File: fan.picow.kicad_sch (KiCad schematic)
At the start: 41 parts, among them U1 PicoW

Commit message: pop stashed changes
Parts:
- removed C2: 0.1uF, Capacitor_SMD:C_0603_1608Metric_Pad1.08x0.95mm_HandSolder, symbol Device:C
- removed D4: LED 12V, LED_SMD:LED_0805_2012Metric_Pad1.15x1.40mm_HandSolder, symbol Device:LED
- removed D8: LED 5V, LED_SMD:LED_0805_2012Metric_Pad1.15x1.40mm_HandSolder, symbol Device:LED
- removed D9: 1N5819, Diode_SMD:D_SMA_Handsoldering, symbol Diode:1N5819
- removed R16: 10K, Resistor_SMD:R_0603_1608Metric_Pad0.98x0.95mm_HandSolder, symbol Device:R
- removed R8: 49.9K, Resistor_SMD:R_0603_1608Metric_Pad0.98x0.95mm_HandSolder, symbol Device:R
- added C10: 0.1uF, Capacitor_SMD:C_0603_1608Metric_Pad1.08x0.95mm_HandSolder, symbol Device:C
- added D9: CDBW140-G, Diode_SMD:D_SOD-123F, symbol CDBW140-G:CDBW140-G
- added LS1: CMT-7525-80-SMT-TR, footprints descargados:XDCR_CMT-7525-80-SMT-TR, symbol CMT-7525-80-SMT-TR:CMT-7525-80-SMT-TR
- added Q1: AOD4184A, footprints descargados:DPAK228P994X240-4N, symbol AOD4184A:AOD4184A
- added Q2: BSS138, Package_TO_SOT_SMD:SOT-23, symbol Transistor_FET:BSS138
- added R23: 1k, Resistor_SMD:R_0603_1608Metric_Pad0.98x0.95mm_HandSolder, symbol Device:R
- added SW1: EG1257, footprints descargados:EG1257, symbol EG1257:EG1257
- D1, D7: footprint LED_SMD:LED_0805_2012Metric_Pad1.15x1.40mm_HandSolder -> digikey-footprints:0805; symbol Device:LED -> dk_LED-Indication-Discrete:LG_R971-KN-1; Category (none) -> Optoelectronics; DK_Datasheet_Link (none) -> https://dammedia.osram.info/media/resource/hires/osram-dam-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; DK_Detail_Page (none) -> /product-detail/en/osram-opto-semiconductors-inc/LG-R971-KN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; Digi-Key_PN (none) -> 475-1410-1-ND; Family (none) -> LED Indication - Discrete; MPN (none) -> LG R971-KN-1; Manufacturer (none) -> OSRAM Opto Semiconductors Inc.; Status (none) -> Active
- D2, D3, D5, D6: footprint Diode_SMD:D_SMA_Handsoldering -> Diode_SMD:D_SOD-123; symbol Diode:1N4148 -> 1N4148W:1N4148W
- TP2: value TestP 3V3 -> 3V3
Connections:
- net 12V: now also D1.1, R12.1, R2.1, R5.1, R9.1
- net 3V3: now also D7.1, SW1.3; no longer D7.2 (A)
- net 5V: now also D9.2
- net BUZZ: now also Q2.1 (G)
- net GND: now also C10.2, Q1.3, Q2.2 (S), SW1.1; no longer C1.2, C3.2, C4.2, C5.2, R1.2, R11.2, R14.2, R4.2, R7.2
- net RELC: now also R23.1
- net TACHM1: now also D2.1; no longer D2.2 (A)
- net TACHM2: now also D3.1; no longer D3.2 (A)
- net TACHM3: now also D5.1; no longer D5.2 (A)
- net TACHM4: now also D6.1; no longer D6.2 (A)
- net VSYS: now also D9.1
- net at R15.1: now also D7.2; no longer D7.1 (K)
- net at R10.2, R11.1: now also D5.2; no longer D5.1 (K)
- net at R3.2, R4.1: now also D2.2; no longer D2.1 (K)
- net at R6.2, R7.1: now also D3.2; no longer D3.1 (K)
- net at R13.2, R14.1: now also D6.2; no longer D6.1 (K)
- net at R1.1: now also D1.2; no longer D1.1 (K)
- removed net 12VFAN: D1.2 (A), R12.1, R2.1, R5.1, R9.1
- new net: LS1.N, Q2.3 (D)
- new net: C10.1, LS1.P, SW1.2
- new net: Q1.1, R23.2
- new net GNDFAN: C1.2, C3.2, C4.2, C5.2, Q1.4, R1.2, R11.2, R14.2, R4.2, R7.2
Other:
- sheet conectores ports: added GNDFAN; removed 12VFAN, BZZ, COM, RELC
- note added: "Buzzer control"
- note added: "Fan control"
- note added: "To match ~240uA for the 12V LEDs, then 20k for 5V and 13.7k for 3.3V would produce more uniform brightness"
- moved on the sheet: C1, C3, C4, C5, C6, H1, H2, H3, H4, R1, R10, R11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

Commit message: remove a comment
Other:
- note removed: "Revisar los C que deben tener polaridad y porqué"
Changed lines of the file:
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@@
     (stroke (width 0) (type default) (color 0 0 0 0))
-  )
-  (text "Revisar los C que deben tener polaridad y porqué" (at 21.59 167.64 0)
-    (effects (font (size 1.27 1.27)) (justify left bottom))
   )
   (text "Fan control" (at 19.685 22.225 0)
@@
   )
   (text "To match ~240uA for the 12V LEDs, then 20k for 5V and 13.7k for 3.3V would produce more uniform brightness\n"
-    (at 21.59 171.45 0)
+    (at 21.59 167.64 0)
     (effects (font (size 1.27 1.27)) (justify left bottom))
   )

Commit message: add text box
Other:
- note added: "Mounting holes"
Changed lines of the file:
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@@
   (no_connect (at 160.02 30.48))
   (no_connect (at 160.02 33.02))
+  (polyline (pts (xy 238.125 136.525) (xy 208.915 136.525))
+    (stroke (width 0) (type default) (color 0 0 0 0))
+  )
   (wire (pts (xy 204.47 58.42) (xy 195.58 58.42))
     (stroke (width 0) (type default) (color 0 0 0 0))
@@
     (stroke (width 0) (type default) (color 0 0 0 0))
   )
+  (polyline (pts (xy 208.915 102.87) (xy 208.915 136.525))
+    (stroke (width 0) (type default) (color 0 0 0 0))
+  )
   (wire (pts (xy 34.925 47.625) (xy 37.465 47.625))
     (stroke (width 0) (type default) (color 0 0 0 0))
@@
     (stroke (width 0) (type default) (color 0 0 0 0))
   )
+  (polyline (pts (xy 208.915 102.87) (xy 238.125 102.87))
+    (stroke (width 0) (type default) (color 0 0 0 0))
+  )
   (wire (pts (xy 65.405 60.325) (xy 65.405 62.865))
     (stroke (width 0) (type default) (color 0 0 0 0))
@@
     (stroke (width 0) (type default) (color 0 0 0 0))
   )
+  (polyline (pts (xy 238.125 102.87) (xy 238.125 136.525))
+    (stroke (width 0) (type default) (color 0 0 0 0))
+  )
   (wire (pts (xy 220.98 57.785) (xy 220.98 60.325))
     (stroke (width 0) (type default) (color 0 0 0 0))
@@
     (stroke (width 0) (type default) (color 0 0 0 0))
   )
+  (text "Mounting holes" (at 210.185 105.41 0)
+    (effects (font (size 1.27 1.27)) (justify left bottom))
+  )
   (text "Fan control" (at 19.685 22.225 0)

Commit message: minor text changes
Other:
- moved on the sheet: H1, H2, H3, H4
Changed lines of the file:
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@@
   (no_connect (at 160.02 30.48))
   (no_connect (at 160.02 33.02))
-  (polyline (pts (xy 238.125 136.525) (xy 208.915 136.525))
+  (polyline (pts (xy 251.46 136.525) (xy 222.25 136.525))
     (stroke (width 0) (type default) (color 0 0 0 0))
   )
@@
     (stroke (width 0) (type default) (color 0 0 0 0))
   )
-  (polyline (pts (xy 208.915 102.87) (xy 208.915 136.525))
+  (polyline (pts (xy 222.25 102.87) (xy 222.25 136.525))
     (stroke (width 0) (type default) (color 0 0 0 0))
   )
@@
     (stroke (width 0) (type default) (color 0 0 0 0))
   )
-  (polyline (pts (xy 208.915 102.87) (xy 238.125 102.87))
+  (polyline (pts (xy 222.25 102.87) (xy 251.46 102.87))
     (stroke (width 0) (type default) (color 0 0 0 0))
   )
@@
     (stroke (width 0) (type default) (color 0 0 0 0))
   )
-  (polyline (pts (xy 238.125 102.87) (xy 238.125 136.525))
+  (polyline (pts (xy 251.46 102.87) (xy 251.46 136.525))
     (stroke (width 0) (type default) (color 0 0 0 0))
   )
@@
     (stroke (width 0) (type default) (color 0 0 0 0))
   )
-  (text "Mounting holes" (at 210.185 105.41 0)
+  (text "Mounting holes" (at 223.52 105.41 0)
     (effects (font (size 1.27 1.27)) (justify left bottom))
   )
@@
     (pin "2")
   )
-  (symbol (lib_id "Mechanical:MountingHole") (at 213.36 116.205 0) (unit 1)
-    (in_bom yes) (on_board yes) (fields_autoplaced)
-    (property "Reference" "H2" (id 0) (at 216.535 114.9349 0)
-      (effects (font (size 1.27 1.27)) (justify left))
-    )
-    (property "Value" "MountingHole" (id 1) (at 216.535 117.4749 0)
-      (effects (font (size 1.27 1.27)) (justify left))
-    )
-    (property "Footprint" "MountingHole:MountingHole_3.2mm_M3" (id 2) (at 213.36 116.205 0)
-      (effects (font (size 1.27 1.27)) hide)
-    )
-    (property "Datasheet" "~" (id 3) (at 213.36 116.205 0)
+  (symbol (lib_id "Mechanical:MountingHole") (at 226.695 116.205 0) (unit 1)
+    (in_bom yes) (on_board yes) (fields_autoplaced)
+    (property "Reference" "H2" (id 0) (at 229.87 114.9349 0)
+      (effects (font (size 1.27 1.27)) (justify left))
+    )
+    (property "Value" "MountingHole" (id 1) (at 229.87 117.4749 0)
+      (effects (font (size 1.27 1.27)) (justify left))
+    )
+    (property "Footprint" "MountingHole:MountingHole_3.2mm_M3" (id 2) (at 226.695 116.205 0)
+      (effects (font (size 1.27 1.27)) hide)
+    )
+    (property "Datasheet" "~" (id 3) (at 226.695 116.205 0)
       (effects (font (size 1.27 1.27)) hide)
     )
@@
     (pin "2")
   )
-  (symbol (lib_id "Mechanical:MountingHole") (at 213.36 121.92 0) (unit 1)
-    (in_bom yes) (on_board yes) (fields_autoplaced)
-    (property "Reference" "H3" (id 0) (at 216.535 120.6499 0)
-      (effects (font (size 1.27 1.27)) (justify left))
-    )
-    (property "Value" "MountingHole" (id 1) (at 216.535 123.1899 0)
-      (effects (font (size 1.27 1.27)) (justify left))
-    )
-    (property "Footprint" "MountingHole:MountingHole_3.2mm_M3" (id 2) (at 213.36 121.92 0)
-      (effects (font (size 1.27 1.27)) hide)
-    )
-    (property "Datasheet" "~" (id 3) (at 213.36 121.92 0)
+  (symbol (lib_id "Mechanical:MountingHole") (at 226.695 121.92 0) (unit 1)
+    (in_bom yes) (on_board yes) (fields_autoplaced)
+    (property "Reference" "H3" (id 0) (at 229.87 120.6499 0)
+      (effects (font (size 1.27 1.27)) (justify left))
+    )
+    (property "Value" "MountingHole" (id 1) (at 229.87 123.1899 0)
+      (effects (font (size 1.27 1.27)) (justify left))
+    )
+    (property "Footprint" "MountingHole:MountingHole_3.2mm_M3" (id 2) (at 226.695 121.92 0)
+      (effects (font (size 1.27 1.27)) hide)
+    )
+    (property "Datasheet" "~" (id 3) (at 226.695 121.92 0)
       (effects (font (size 1.27 1.27)) hide)
     )
@@
     (pin "2")
   )
-  (symbol (lib_id "power:GND") (at 213.36 132.08 0) (unit 1)
-    (in_bom yes) (on_board yes)
-    (property "Reference" "#PWR03" (id 0) (at 213.36 138.43 0)
-      (effects (font (size 1.27 1.27)) hide)
-    )
-    (property "Value" "GND" (id 1) (at 217.17 132.08 0))
-    (property "Footprint" "" (id 2) (at 213.36 132.08 0)
-      (effects (font (size 1.27 1.27)) hide)
-    )
-    (property "Datasheet" "" (id 3) (at 213.36 132.08 0)
+  (symbol (lib_id "power:GND") (at 226.695 132.08 0) (unit 1)
+    (in_bom yes) (on_board yes)
+    (property "Reference" "#PWR03" (id 0) (at 226.695 138.43 0)
+      (effects (font (size 1.27 1.27)) hide)
+    )
+    (property "Value" "GND" (id 1) (at 230.505 132.08 0))
+    (property "Footprint" "" (id 2) (at 226.695 132.08 0)
+      (effects (font (size 1.27 1.27)) hide)
+    )
+    (property "Datasheet" "" (id 3) (at 226.695 132.08 0)
       (effects (font (size 1.27 1.27)) hide)
     )
@@
     (pin "2")
   )
-  (symbol (lib_id "Mechanical:MountingHole_Pad") (at 213.36 129.54 0) (unit 1)
-    (in_bom yes) (on_board yes) (fields_autoplaced)
-    (property "Reference" "H4" (id 0) (at 216.535 126.9999 0)
-      (effects (font (size 1.27 1.27)) (justify left))
-    )
-    (property "Value" "MountingHole_Pad" (id 1) (at 216.535 129.5399 0)
-      (effects (font (size 1.27 1.27)) (justify left))
-    )
-    (property "Footprint" "MountingHole:MountingHole_3.2mm_M3_Pad_Via" (id 2) (at 213.36 129.54 0)
-      (effects (font (size 1.27 1.27)) hide)
-    )
-    (property "Datasheet" "~" (id 3) (at 213.36 129.54 0)
+  (symbol (lib_id "Mechanical:MountingHole_Pad") (at 226.695 129.54 0) (unit 1)
+    (in_bom yes) (on_board yes) (fields_autoplaced)
+    (property "Reference" "H4" (id 0) (at 229.87 126.9999 0)
+      (effects (font (size 1.27 1.27)) (justify left))
+    )
+    (property "Value" "MountingHole_Pad" (id 1) (at 229.87 129.5399 0)
+      (effects (font (size 1.27 1.27)) (justify left))
+    )
+    (property "Footprint" "MountingHole:MountingHole_3.2mm_M3_Pad_Via" (id 2) (at 226.695 129.54 0)
+      (effects (font (size 1.27 1.27)) hide)
+    )
+    (property "Datasheet" "~" (id 3) (at 226.695 129.54 0)
       (effects (font (size 1.27 1.27)) hide)
     )
@@
     (pin "2")
   )
-  (symbol (lib_id "Mechanical:MountingHole") (at 213.36 109.855 0) (unit 1)
-    (in_bom yes) (on_board yes) (fields_autoplaced)
-    (property "Reference" "H1" (id 0) (at 216.535 108.5849 0)
-      (effects (font (size 1.27 1.27)) (justify left))
-    )
-    (property "Value" "MountingHole" (id 1) (at 216.535 111.1249 0)
-      (effects (font (size 1.27 1.27)) (justify left))
-    )
-    (property "Footprint" "MountingHole:MountingHole_3.2mm_M3" (id 2) (at 213.36 109.855 0)
-      (effects (font (size 1.27 1.27)) hide)
-    )
-    (property "Datasheet" "~" (id 3) (at 213.36 109.855 0)
+  (symbol (lib_id "Mechanical:MountingHole") (at 226.695 109.855 0) (unit 1)
+    (in_bom yes) (on_board yes) (fields_autoplaced)
+    (property "Reference" "H1" (id 0) (at 229.87 108.5849 0)
+      (effects (font (size 1.27 1.27)) (justify left))
+    )
+    (property "Value" "MountingHole" (id 1) (at 229.87 111.1249 0)
+      (effects (font (size 1.27 1.27)) (justify left))
+    )
+    (property "Footprint" "MountingHole:MountingHole_3.2mm_M3" (id 2) (at 226.695 109.855 0)
+      (effects (font (size 1.27 1.27)) hide)
+    )
+    (property "Datasheet" "~" (id 3) (at 226.695 109.855 0)
       (effects (font (size 1.27 1.27)) hide)
     )
@@
     )
     (path "/86e12817-80ac-414c-aa23-eca04293b568/1790f650-74c6-4ab3-b8d8-2a95be562786"
-      (reference "J2") (unit 1) (value "Fan1 Conn") (footprint "Connector:FanPinHeader_1x04_P2.54mm_Vertical")
+      (reference "J2") (unit 1) (value "Fan1") (footprint "Connector:FanPinHeader_1x04_P2.54mm_Vertical")
     )
     (path "/86e12817-80ac-414c-aa23-eca04293b568/816bec53-7040-496e-8792-50c0d8fdfc35"
-      (reference "J3") (unit 1) (value "Fan2 Conn") (footprint "Connector:FanPinHeader_1x04_P2.54mm_Vertical")
+      (reference "J3") (unit 1) (value "Fan2") (footprint "Connector:FanPinHeader_1x04_P2.54mm_Vertical")
     )
     (path "/86e12817-80ac-414c-aa23-eca04293b568/e27b30b1-7f61-4163-abe6-653e2b466f00"
-      (reference "J4") (unit 1) (value "Fan4 Conn") (footprint "Connector:FanPinHeader_1x04_P2.54mm_Vertical")
+      (reference "J4") (unit 1) (value "Fan4") (footprint "Connector:FanPinHeader_1x04_P2.54mm_Vertical")
     )
     (path "/86e12817-80ac-414c-aa23-eca04293b568/5735702d-5289-43a6-9aa8-c25bf1ef4005"
-      (reference "J5") (unit 1) (value "Fan3 Conn") (footprint "Connector:FanPinHeader_1x04_P2.54mm_Vertical")
+      (reference "J5") (unit 1) (value "Fan3") (footprint "Connector:FanPinHeader_1x04_P2.54mm_Vertical")
     )
     (path "/86e12817-80ac-414c-aa23-eca04293b568/8b6c6ee4-7500-4b7b-b294-9ce1b523ab35"

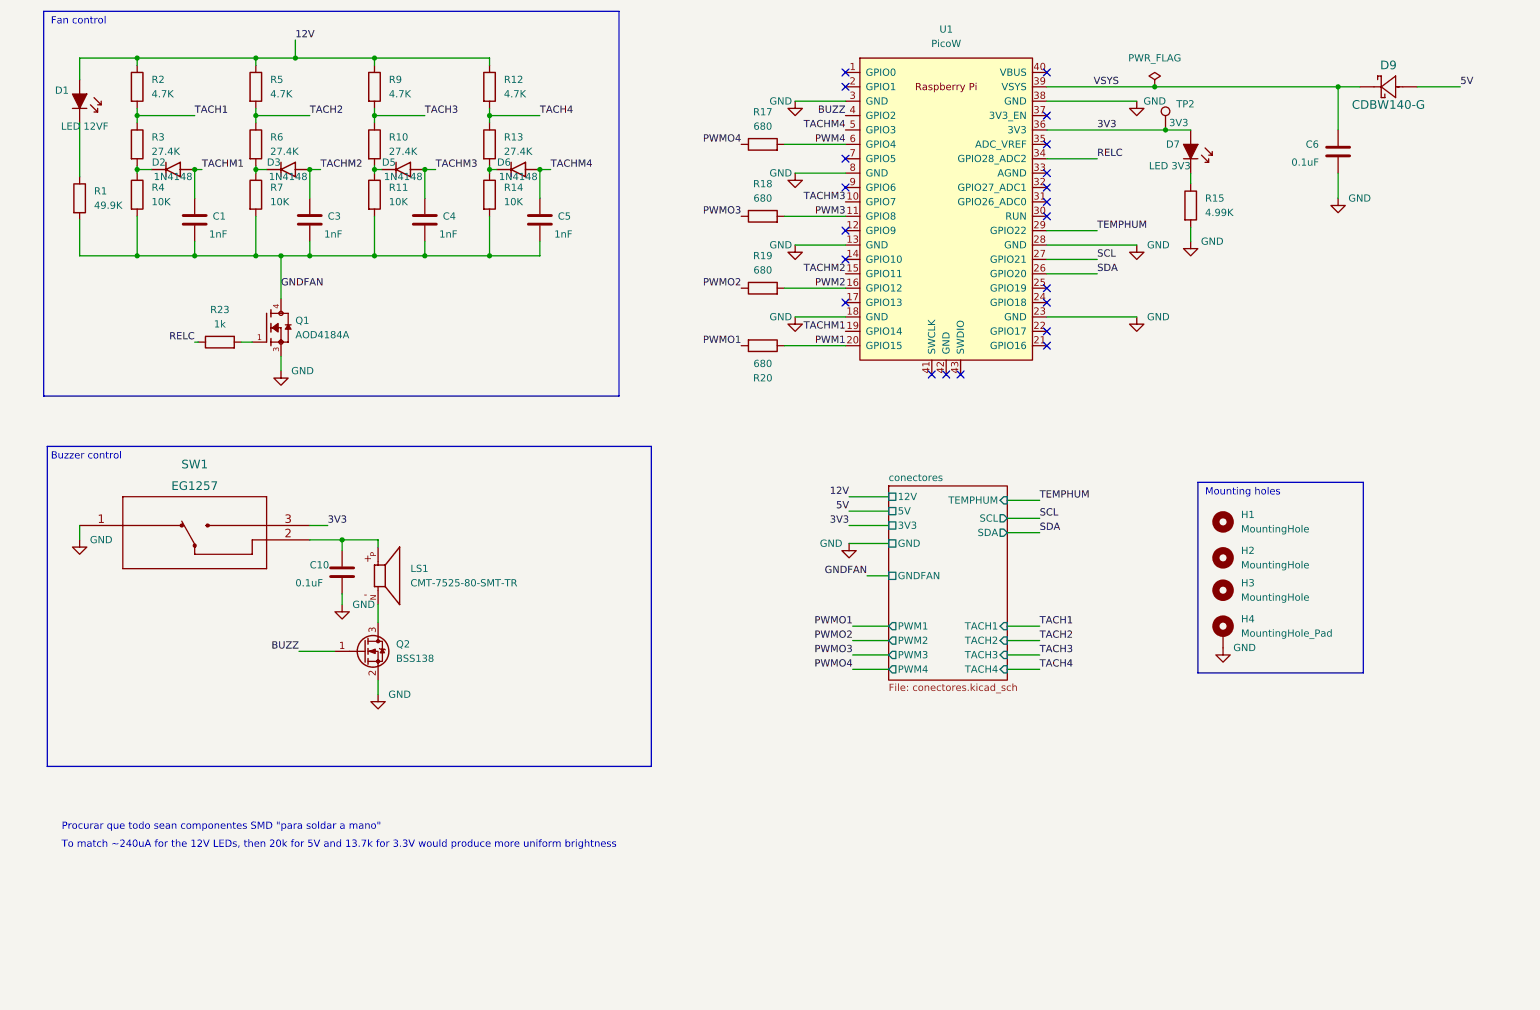
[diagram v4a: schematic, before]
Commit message: add drive high-side switch
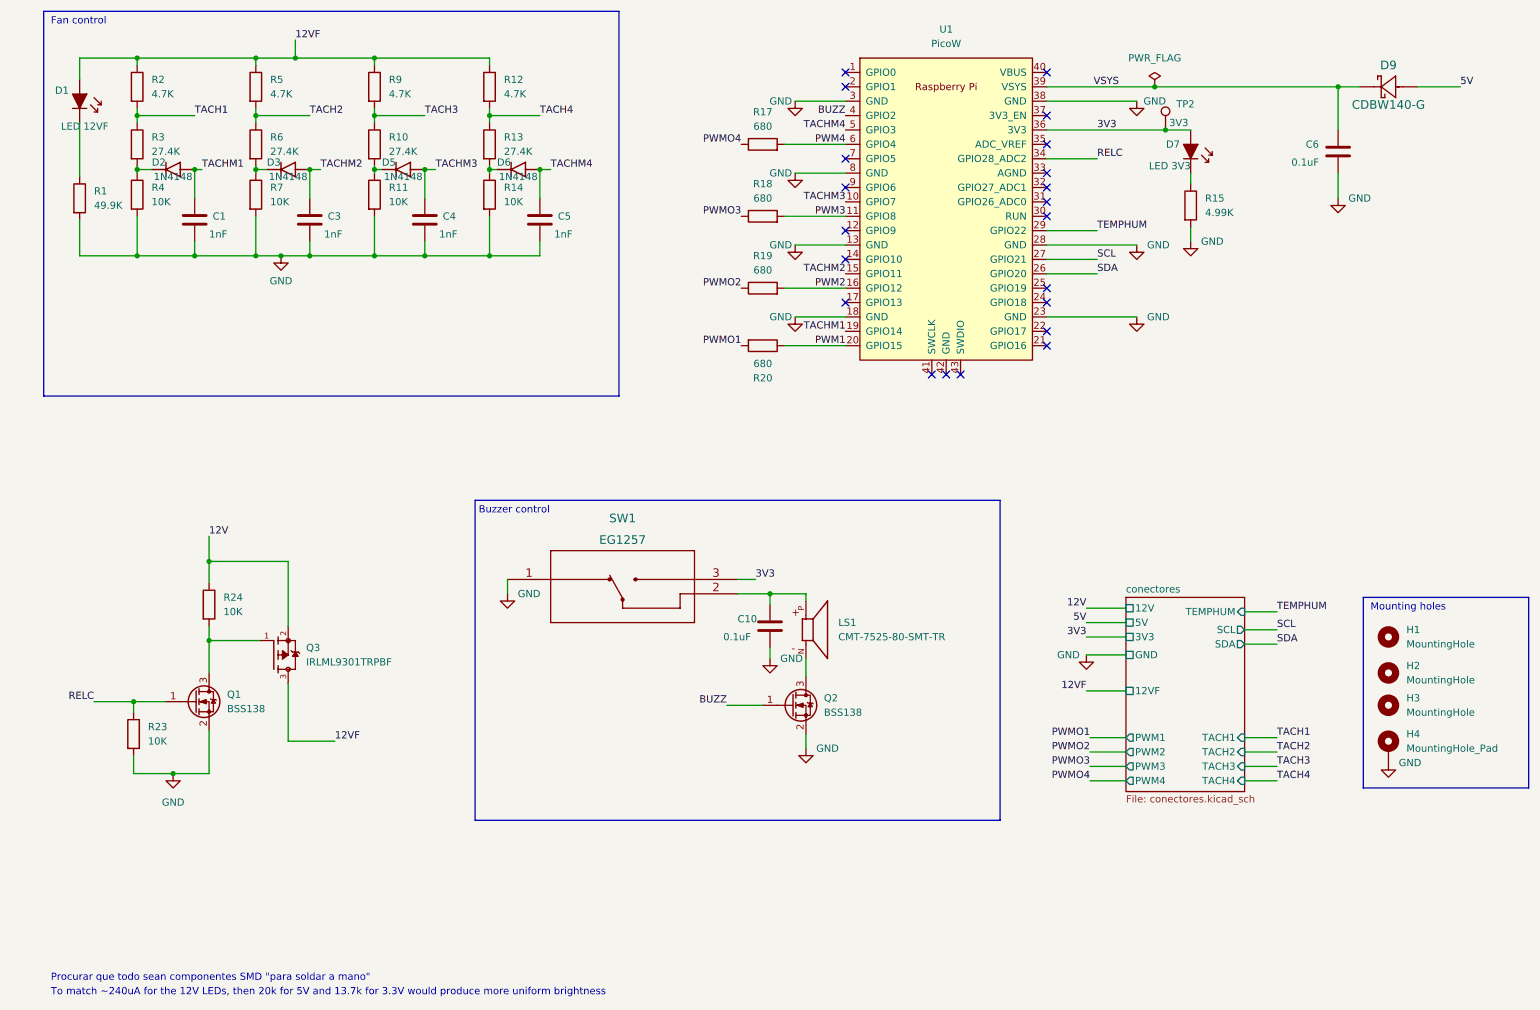
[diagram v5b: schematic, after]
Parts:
- removed Q1: AOD4184A, footprints descargados:DPAK228P994X240-4N, symbol AOD4184A:AOD4184A
- added Q1: BSS138, Package_TO_SOT_SMD:SOT-23, symbol Transistor_FET:BSS138
- added Q3: IRLML9301TRPBF, footprints descargados:IRLML9301TRPBF.SOT95P237X112-3N, symbol IRLML9301TRPBF:IRLML9301TRPBF
- added R24: 10K, Resistor_SMD:R_0603_1608Metric_Pad0.98x0.95mm_HandSolder, symbol Device:R
- R23: value 1k -> 10K
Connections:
- net GNDFAN is gone; now on net GND: C1.2, C3.2, C4.2, C5.2, R1.2, R11.2, R14.2, R4.2, R7.2
- net 12V: now also Q3.2, R24.1; no longer D1.1, R12.1, R2.1, R5.1, R9.1
- net GND: now also R23.2, Q1.2 (S)
- net RELC: now also Q1.1 (G)
- new net: Q1.3 (D), Q3.1, R24.2
- new net 12VF: D1.1, Q3.3, R12.1, R2.1, R5.1, R9.1
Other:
- sheet conectores ports: added 12VF; removed GNDFAN
- moved on the sheet: C10, H1, H2, H3, H4, LS1, Q2, SW1
